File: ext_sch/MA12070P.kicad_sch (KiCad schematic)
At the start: 49 parts, among them J7 Screw Term.

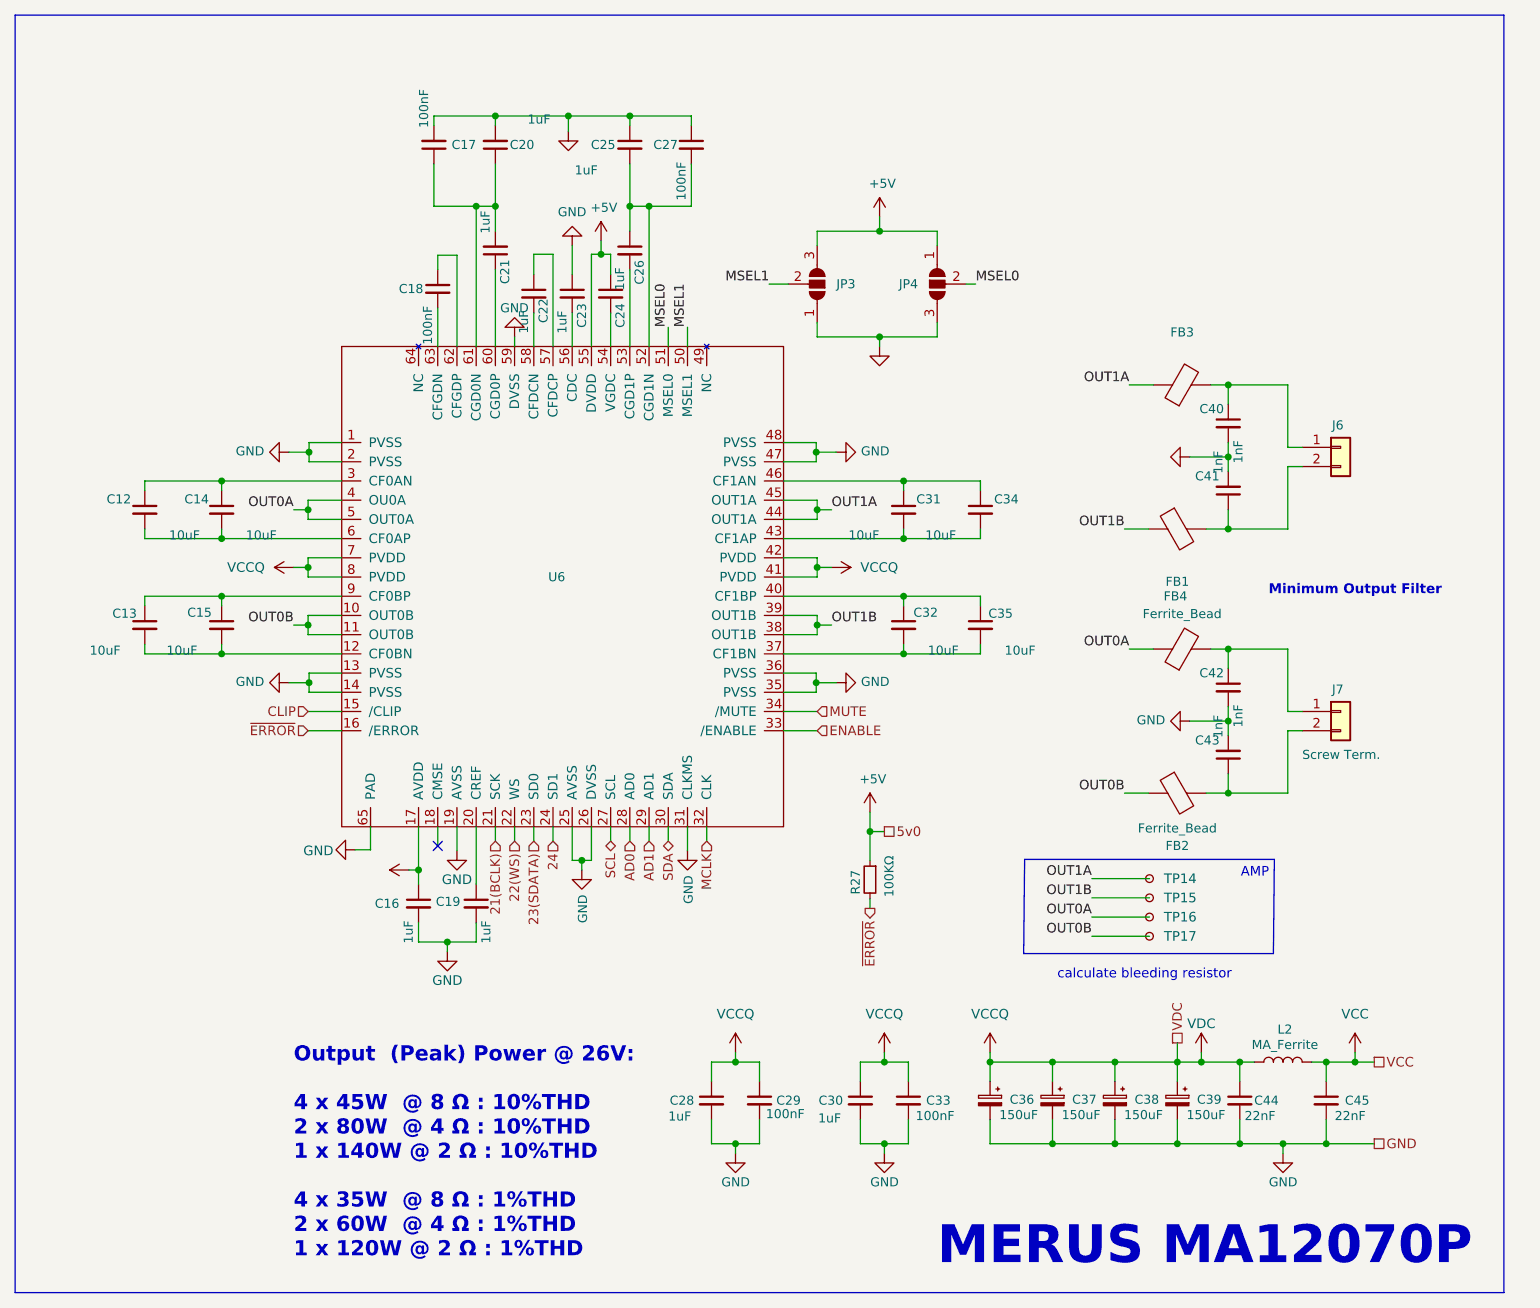
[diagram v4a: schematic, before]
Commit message: fix: incorrect subschematic path
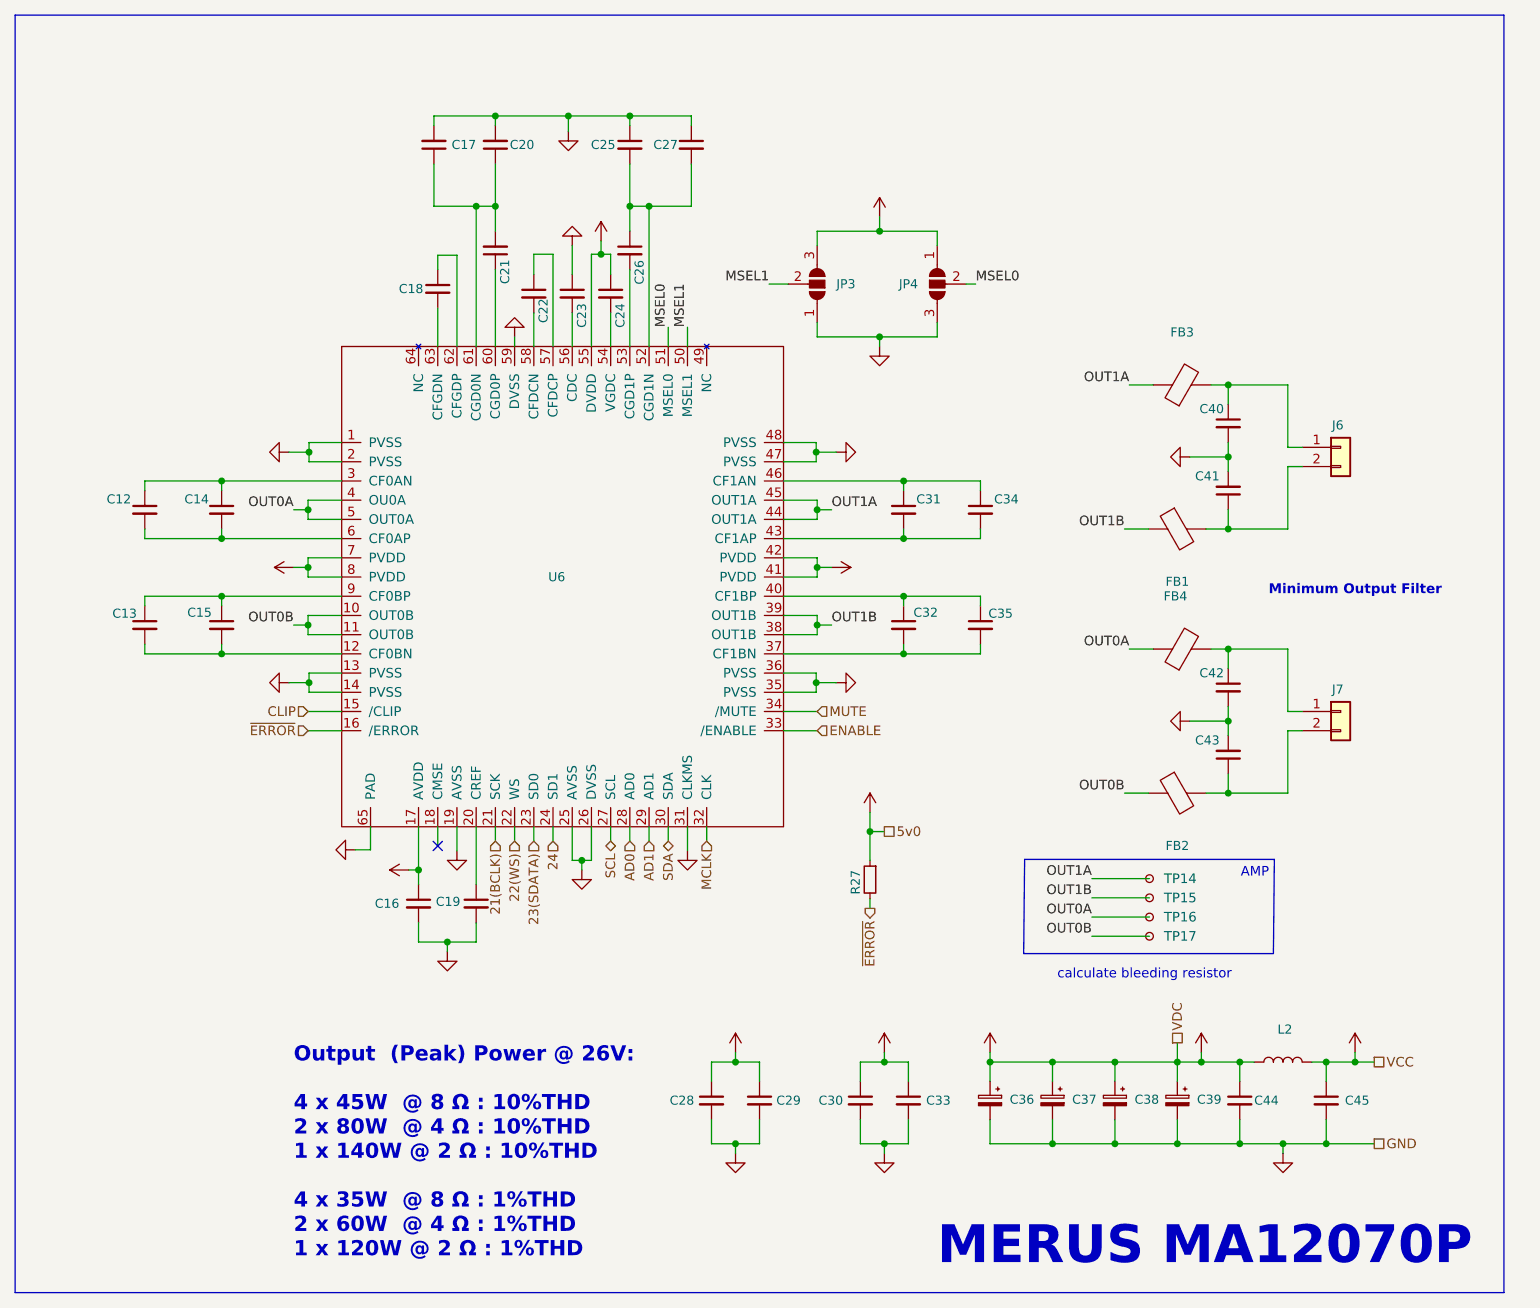
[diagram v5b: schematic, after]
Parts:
- C12, C13, C14, C15, C31, C32, C34, C35: value 10uF -> (none); footprint Capacitor_SMD:C_0805_2012Metric -> (none)
- C16, C19, C21, C22, C23, C24, C26: value 1uF -> (none); footprint Capacitor_SMD:C_0603_1608Metric -> (none)
- C17, C18, C27, C29, C33: value 100nF -> (none); footprint Capacitor_SMD:C_0603_1608Metric -> (none)
- C20, C25, C28, C30: value 1uF -> (none); footprint Capacitor_SMD:C_0805_2012Metric -> (none)
- C36, C37, C38, C39: value 150uF -> (none); footprint Capacitor_SMD:CP_Elec_8x10 -> (none)
- C40, C41, C42, C43: value 1nF -> (none); footprint Capacitor_SMD:C_0603_1608Metric -> (none)
- C44, C45: value 22nF -> (none); footprint Capacitor_SMD:C_0603_1608Metric -> (none)
- FB1, FB3: value ~ -> (none); footprint Capacitor_SMD:C_1206_3216Metric -> (none)
- FB2, FB4: value Ferrite_Bead -> (none); footprint Capacitor_SMD:C_1206_3216Metric -> (none)
- J6: value ~ -> (none); footprint Lib:Phoenix1989447 -> (none)
- J7: value Screw Term. -> (none); footprint Lib:Phoenix1989447 -> (none)
- JP3, JP4: value ~ -> (none); footprint Jumper:SolderJumper-3_P1.3mm_Bridged12_RoundedPad1.0x1.5mm -> (none)
- L2: value MA_Ferrite -> (none); footprint Lib:MA_Ferrite -> (none)
- R27: value 100KΩ -> (none); footprint Resistor_SMD:R_0603_1608Metric -> (none)
- TP14, TP15, TP16, TP17: value TestPoint_Small -> (none); footprint TestPoint:TestPoint_Pad_D1.5mm -> (none)
- U6: value ~ -> (none); footprint Package_DFN_QFN:QFN-64-1EP_9x9mm_P0.5mm_EP5.45x5.45mm_ThermalVias -> (none)

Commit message: Rerouted a couple of small things pr. @feelfreelinux request
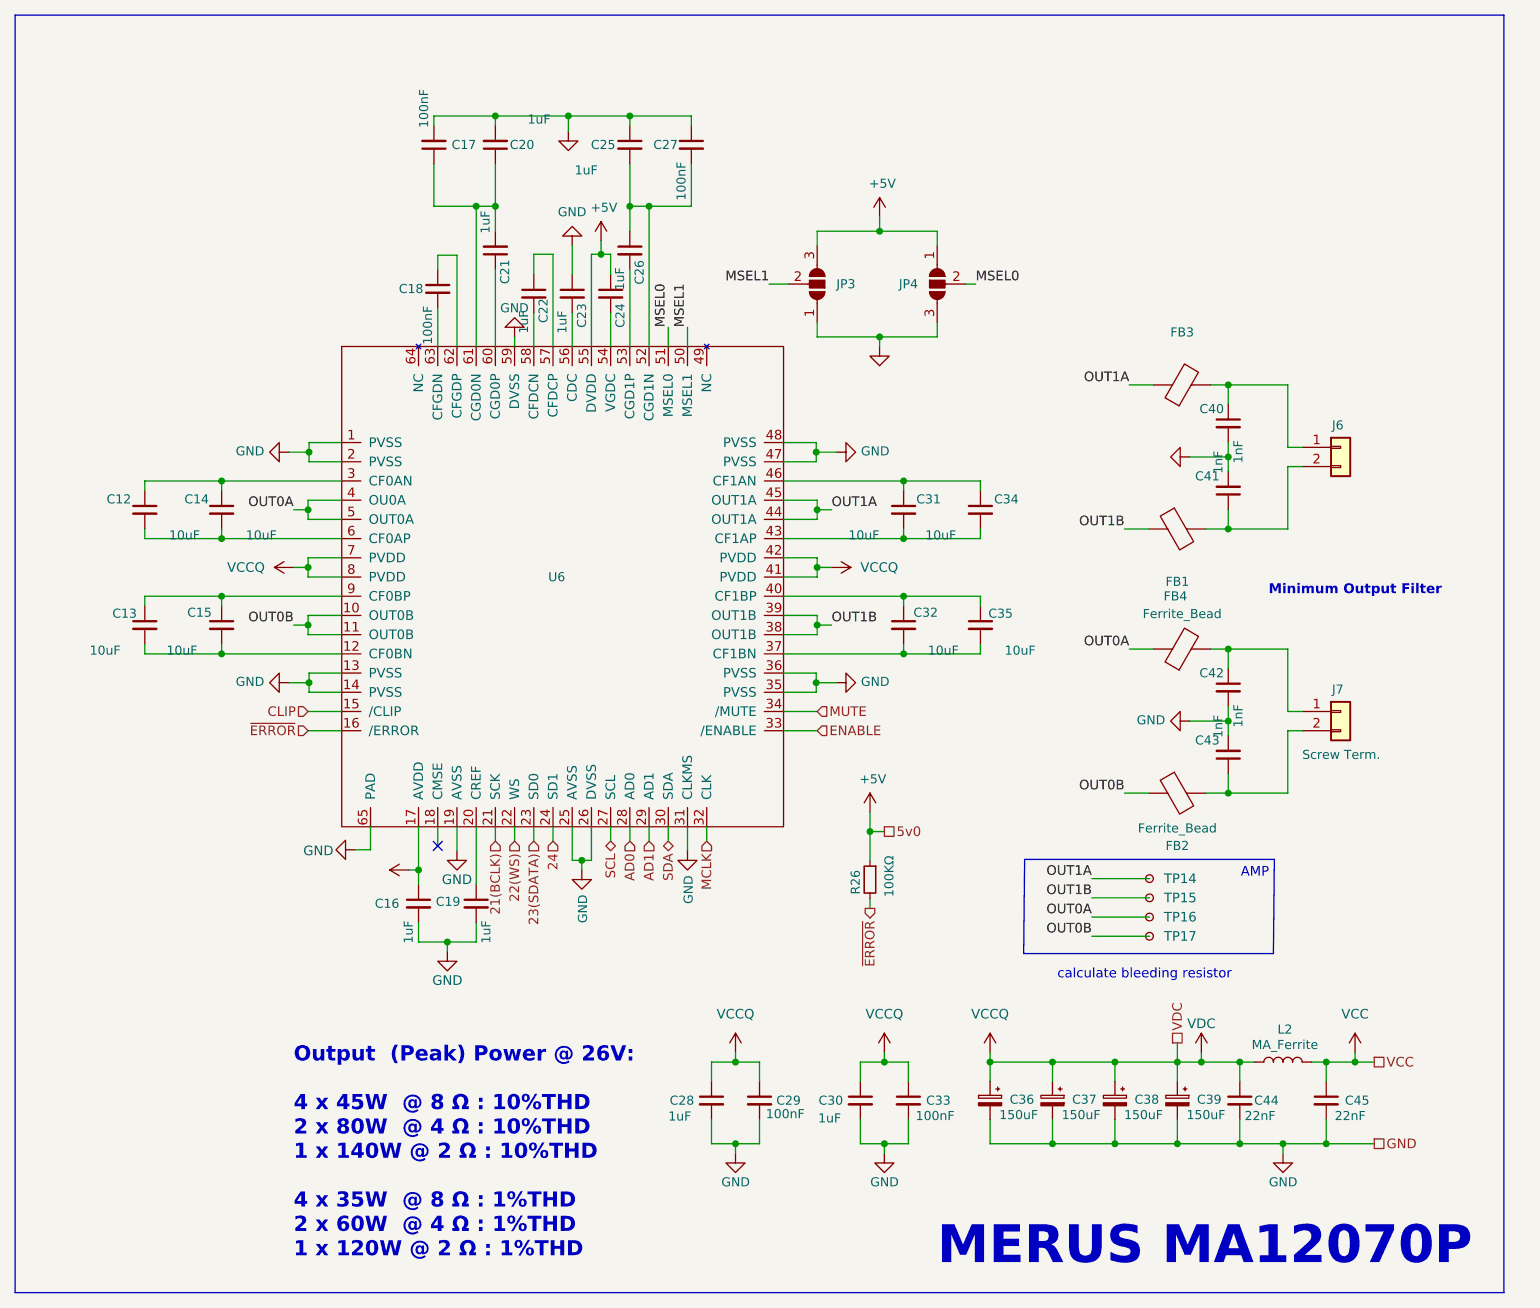
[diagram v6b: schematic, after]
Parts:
- C12, C13, C14, C15, C31, C32, C34, C35: value (none) -> 10uF; footprint (none) -> Capacitor_SMD:C_0805_2012Metric
- C16, C19, C21, C22, C23, C24, C26: value (none) -> 1uF; footprint (none) -> Capacitor_SMD:C_0603_1608Metric
- C17, C18, C27, C29, C33: value (none) -> 100nF; footprint (none) -> Capacitor_SMD:C_0603_1608Metric
- C20, C25, C28, C30: value (none) -> 1uF; footprint (none) -> Capacitor_SMD:C_0805_2012Metric
- C36, C37, C38, C39: value (none) -> 150uF; footprint (none) -> Capacitor_SMD:CP_Elec_8x10
- C40, C41, C42, C43: value (none) -> 1nF; footprint (none) -> Capacitor_SMD:C_0603_1608Metric
- C44, C45: value (none) -> 22nF; footprint (none) -> Capacitor_SMD:C_0603_1608Metric
- FB1, FB3: value (none) -> ~; footprint (none) -> Capacitor_SMD:C_1206_3216Metric
- FB2, FB4: value (none) -> Ferrite_Bead; footprint (none) -> Capacitor_SMD:C_1206_3216Metric
- J6: value (none) -> ~; footprint (none) -> Lib:Phoenix1989447
- J7: value (none) -> Screw Term.; footprint (none) -> Lib:Phoenix1989447
- JP3, JP4: value (none) -> ~; footprint (none) -> Jumper:SolderJumper-3_P1.3mm_Bridged12_RoundedPad1.0x1.5mm
- L2: value (none) -> MA_Ferrite; footprint (none) -> Lib:MA_Ferrite
- R26: renamed from R27; value (none) -> 100KΩ; footprint (none) -> Resistor_SMD:R_0603_1608Metric
- TP14, TP15, TP16, TP17: value (none) -> TestPoint_Small; footprint (none) -> TestPoint:TestPoint_Pad_D1.5mm
- U6: value (none) -> ~; footprint (none) -> Package_DFN_QFN:QFN-64-1EP_9x9mm_P0.5mm_EP5.45x5.45mm_ThermalVias

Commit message: Small cosmetic changes to both PCB and SCH
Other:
- moved on the sheet: C12, C13, C14, C15, C16, C17, C18, C19, C20, C21, C22, C23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

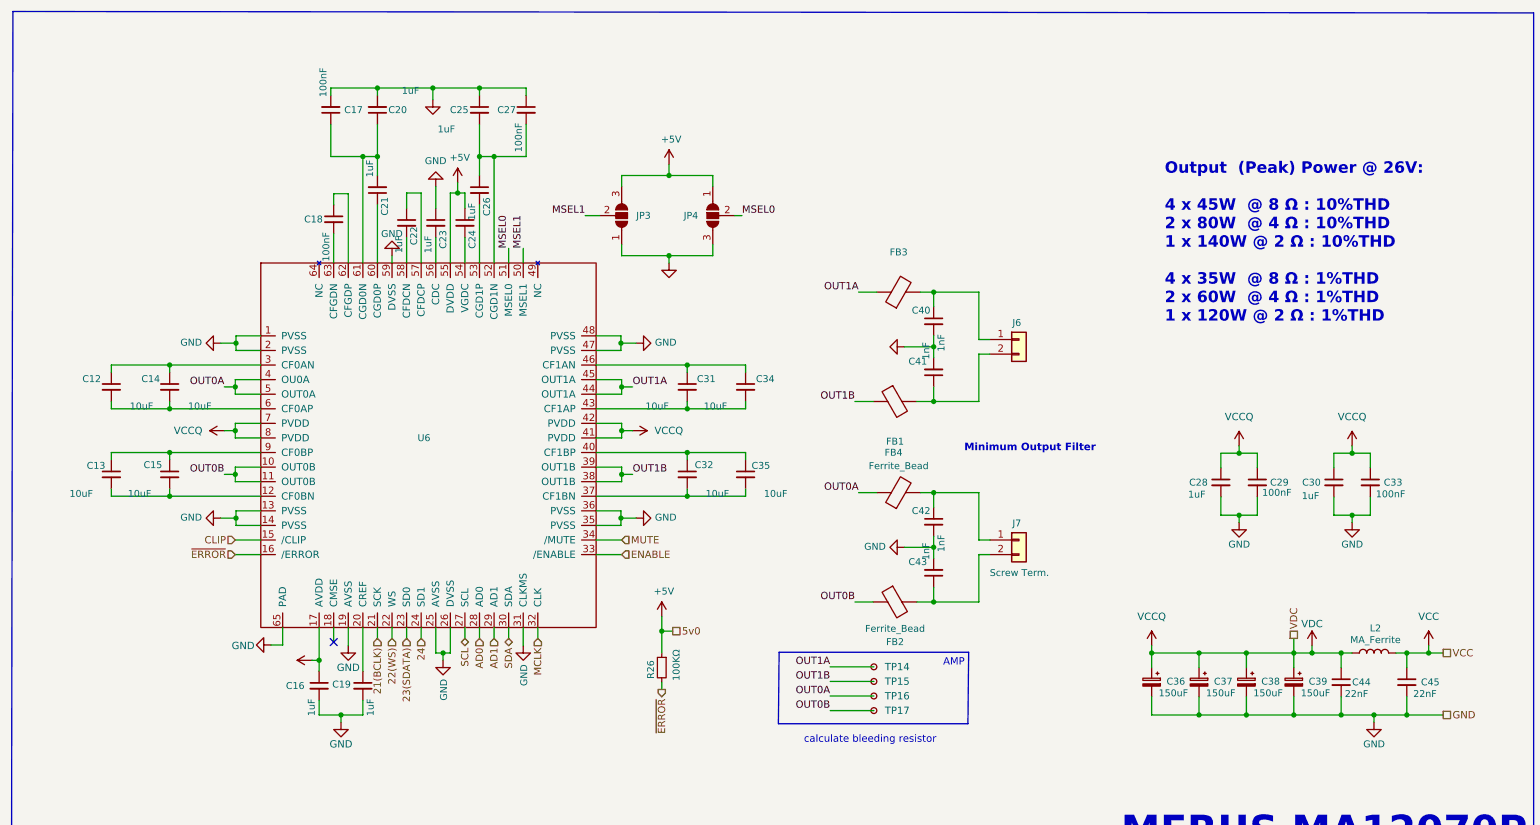
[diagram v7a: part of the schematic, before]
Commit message: Updated all schematic values and parts numbers
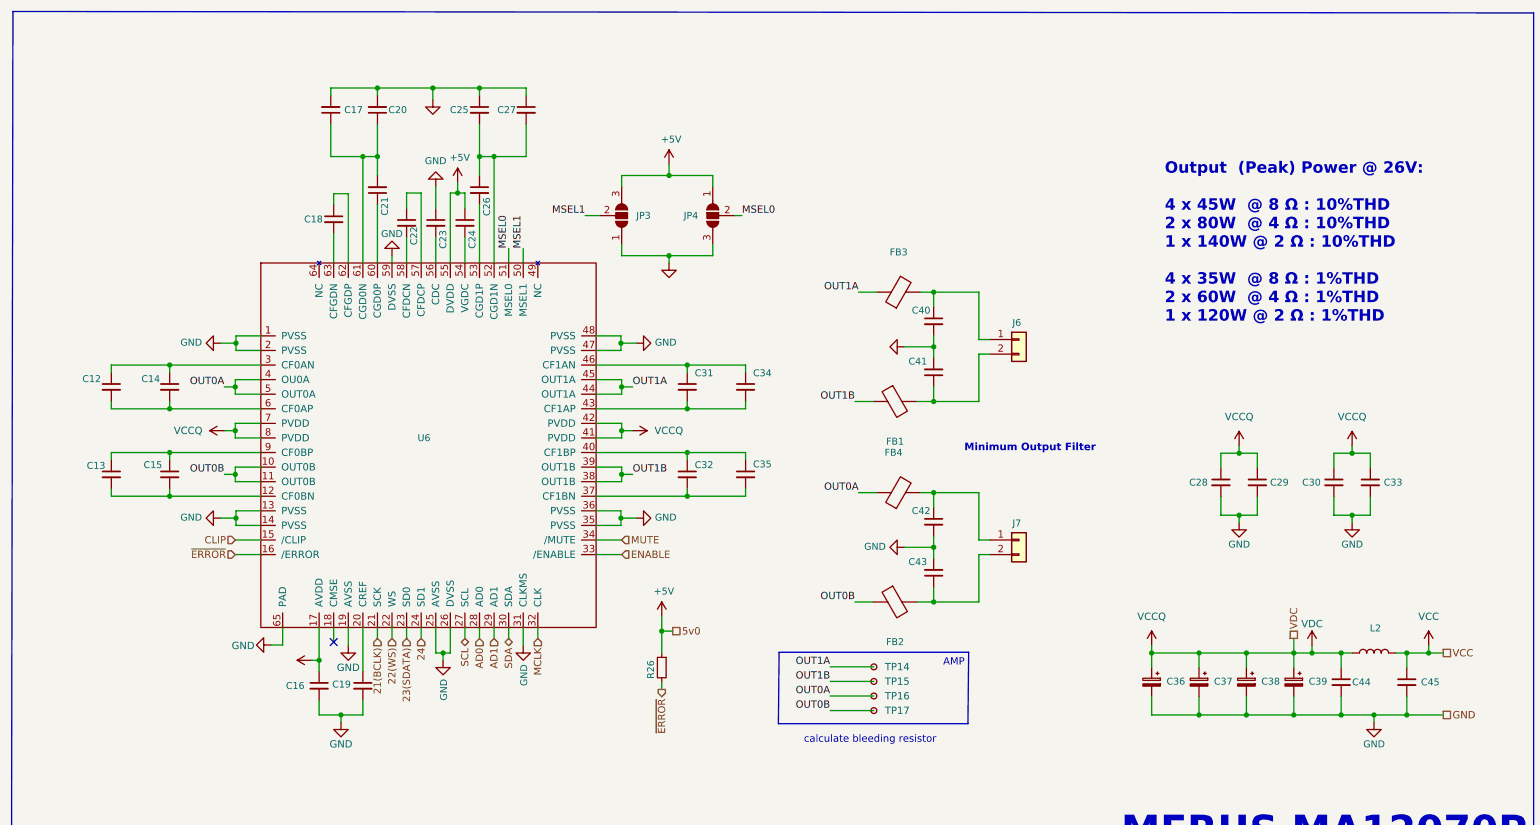
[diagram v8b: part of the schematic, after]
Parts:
- C12, C13, C14, C15, C31, C32, C34, C35: value 10uF -> (none); footprint Capacitor_SMD:C_0805_2012Metric -> (none)
- C16, C19, C21, C22, C23, C24, C26: value 1uF -> (none); footprint Capacitor_SMD:C_0603_1608Metric -> (none)
- C17, C18, C27, C29, C33: value 100nF -> (none); footprint Capacitor_SMD:C_0603_1608Metric -> (none)
- C20, C25, C28, C30: value 1uF -> (none); footprint Capacitor_SMD:C_0805_2012Metric -> (none)
- C36, C37, C38, C39: value 150uF -> (none); footprint Capacitor_SMD:CP_Elec_8x10 -> (none)
- C40, C41, C42, C43: value 1nF -> (none); footprint Capacitor_SMD:C_0603_1608Metric -> (none)
- C44, C45: value 22nF -> (none); footprint Capacitor_SMD:C_0603_1608Metric -> (none)
- FB1, FB3: value ~ -> (none); footprint Capacitor_SMD:C_1206_3216Metric -> (none)
- FB2, FB4: value Ferrite_Bead -> (none); footprint Capacitor_SMD:C_1206_3216Metric -> (none)
- J6: value ~ -> (none); footprint Lib:Phoenix1989447 -> (none)
- J7: value Screw Term. -> (none); footprint Lib:Phoenix1989447 -> (none)
- JP3, JP4: value ~ -> (none); footprint Jumper:SolderJumper-3_P1.3mm_Bridged12_RoundedPad1.0x1.5mm -> (none)
- L2: value MA_Ferrite -> (none); footprint Lib:MA_Ferrite -> (none)
- R26: value 100KΩ -> (none); footprint Resistor_SMD:R_0603_1608Metric -> (none); LCSC C25803 -> C2906980
- TP14, TP15, TP16, TP17: value TestPoint_Small -> (none); footprint TestPoint:TestPoint_Pad_D1.5mm -> (none)
- U6: value ~ -> (none); footprint Package_DFN_QFN:QFN-64-1EP_9x9mm_P0.5mm_EP5.45x5.45mm_ThermalVias -> (none)
